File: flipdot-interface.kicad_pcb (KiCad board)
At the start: 4 copper layers, 109.2 x 88.9 mm, 100 parts, among them J1 Conn_02x30_Odd_Even, J2 Conn_02x06_Odd_Even, J3 Screw_Terminal_01x04, J4 Conn_02x06_Odd_Even, U10 74LVC1G19, U11 74HCT595, U12 ULN2803A, U13 74HCT244, U14 LM2734Y, U15 AP1117-33, U16 tle75080-esd, U17 tle75080-esd, U18 tle75080-esd, U4 74HCT595, U5 74HCT595, U6 74HCT595, U7 ULN2803A, U8 ULN2803A, U9 ULN2803A

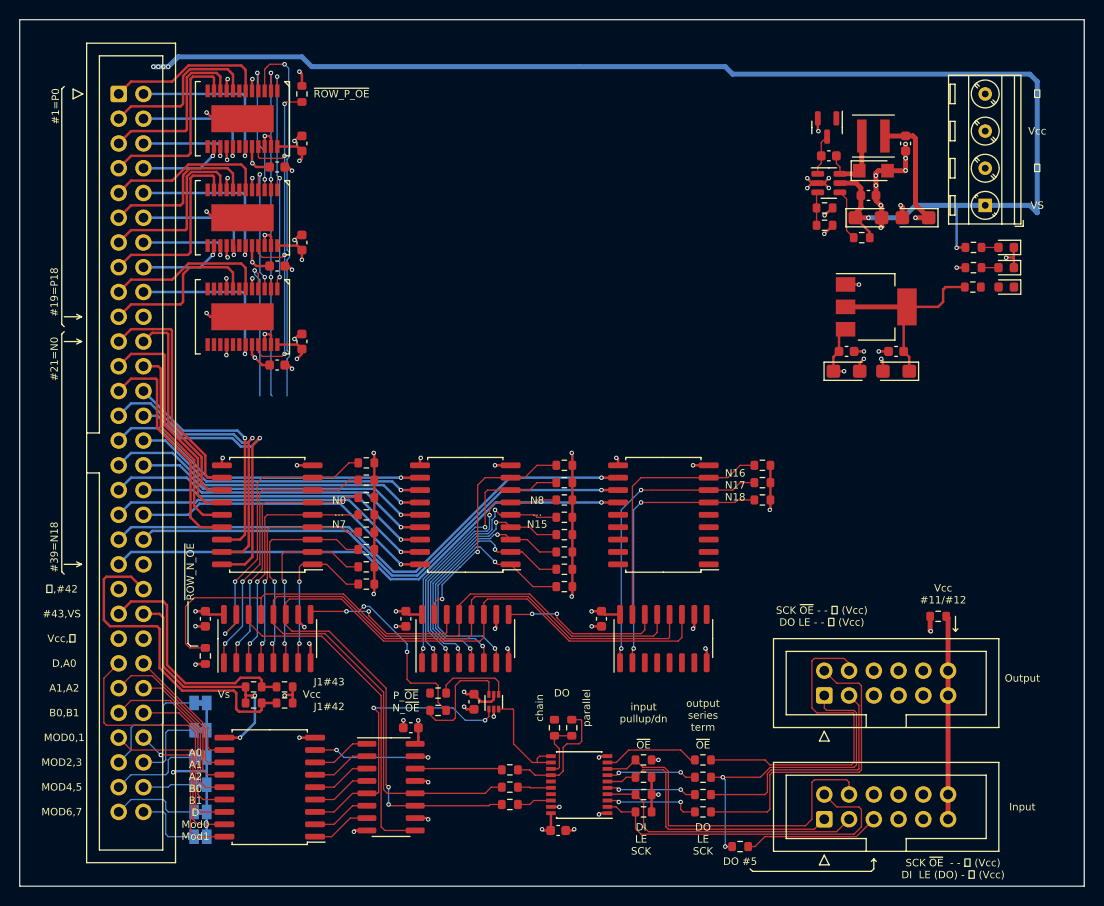
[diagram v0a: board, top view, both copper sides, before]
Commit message: Change negative drivers to a TLE75008-ESD, octal low side driver.
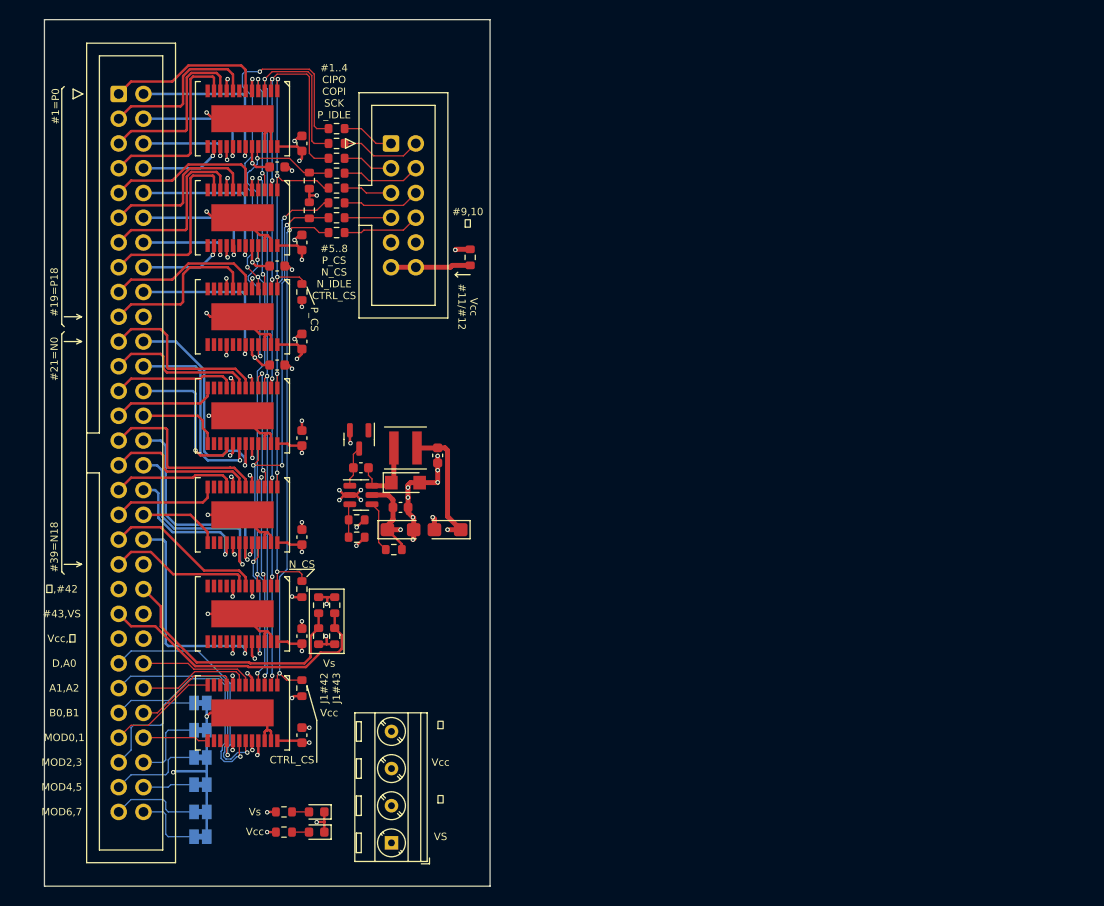
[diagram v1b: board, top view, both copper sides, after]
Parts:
- removed C10, C17, C8, C9: 100n, Capacitor_SMD:C_0603_1608Metric
- removed C16, C18: 10u, Capacitor_Tantalum_SMD:CP_EIA-3216-18_Kemet-A
- removed D24: LED, LED_SMD:LED_0603_1608Metric
- removed J2: Conn_02x06_Odd_Even, Connector_IDC:IDC-Header_2x06_P2.54mm_Vertical
- removed R100, R101, R102, R103, R104, R87, R88, R89, R90: 68R, Resistor_SMD:R_0603_1608Metric
- removed R105, R106, R108: 0R (dnp), Resistor_SMD:R_0603_1608Metric
- removed R58, R59, R60, R61, R62, R63, R64, R65, R66, R67, R68, R69, R70, R71, R72, R73, R74, R75, R76, R77, R78, R96, R97, R98, R99: 10k, Resistor_SMD:R_0603_1608Metric
- removed R79: 1k, Resistor_SMD:R_0603_1608Metric
- removed U10: 74LVC1G19, Package_TO_SOT_SMD:SOT-563
- removed U11, U5, U6: 74HCT595, Package_SO:SOIC-16_3.9x9.9mm_P1.27mm
- removed U12, U7, U8, U9: ULN2803A, Package_SO:SOIC-18W_7.5x11.6mm_P1.27mm
- removed U13: 74HCT244, Package_SO:SSOP-20_4.4x6.5mm_P0.65mm
- removed U15: AP1117-33, Package_TO_SOT_SMD:SOT-223-3_TabPin2
- added R1: 10k, Resistor_SMD:R_0603_1608Metric, F.Cu at (146.6, 59.7)
- added R10: 10k, Resistor_SMD:R_0603_1608Metric, F.Cu at (145.8, 71.1)
- added R11: 10k, Resistor_SMD:R_0603_1608Metric, F.Cu at (145.8, 101.6)
- added R12: 10k, Resistor_SMD:R_0603_1608Metric, F.Cu at (146.6, 62.7)
- added R13: 10k, Resistor_SMD:R_0603_1608Metric, F.Cu at (145.8, 111.8)
- added R2: 68R, Resistor_SMD:R_0603_1608Metric, F.Cu at (149.4, 54.4)
- added R3: 68R, Resistor_SMD:R_0603_1608Metric, F.Cu at (149.4, 58.9)
- added R4: 68R, Resistor_SMD:R_0603_1608Metric, F.Cu at (149.4, 55.9)
- added R5: 68R, Resistor_SMD:R_0603_1608Metric, F.Cu at (149.4, 57.4)
- added R6: 68R, Resistor_SMD:R_0603_1608Metric, F.Cu at (149.4, 60.5)
- added R7: 68R, Resistor_SMD:R_0603_1608Metric, F.Cu at (149.4, 62.0)
- added R8: 68R, Resistor_SMD:R_0603_1608Metric, F.Cu at (149.4, 63.5)
- added R9: 68R, Resistor_SMD:R_0603_1608Metric, F.Cu at (149.4, 65.0)
- added U1: tle75008-esd, vogelchr_package_so:Infineon-PG-TSDSO-24-51, F.Cu at (139.7, 83.8)
- added U2: tle75008-esd, vogelchr_package_so:Infineon-PG-TSDSO-24-51, F.Cu at (139.7, 94.0)
- added U3: tle75008-esd, vogelchr_package_so:Infineon-PG-TSDSO-24-51, F.Cu at (139.7, 104.1)
- U4: value 74HCT595 -> tle75008-esd; footprint Package_SO:SOIC-16_3.9x9.9mm_P1.27mm -> vogelchr_package_so:Infineon-PG-TSDSO-24-51
- moved D22 91.4 mm to (147.3, 124.5)
- moved D23 91.4 mm to (147.3, 126.5)
- moved R94 91.4 mm to (144.0, 124.5)
- moved R95 91.4 mm to (144.0, 126.5)
- moved J3 89.4 mm to (155.0, 127.6)
- moved J4 72.0 mm to (154.9, 55.9), turned to 0 degrees
- moved R107 60.5 mm to (163.1, 67.6), turned to -90 degrees
- moved C11 57.7 mm to (155.9, 93.2)
- moved C12 57.7 mm to (155.9, 95.5)
- moved C13 57.7 mm to (151.8, 89.2)
- moved C14 57.7 mm to (159.7, 87.9)
- moved C15 57.7 mm to (160.7, 95.5)
- moved D20 57.7 mm to (151.7, 86.2)
- moved D21 57.7 mm to (156.4, 90.7)
- moved L1 57.7 mm to (156.4, 87.1)
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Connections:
- net /Row Drivers Positive/~{ROW_P_CS} renamed /~{ROW_P_CS}
- net /~{ROW_P_OE} renamed /ROW_P_IDLE
- J4 pad 1: /DO -> Net-(J4-Pad1)
- J4 pad 11: Net-(J2-Pad11) -> Net-(J4-Pad11)
- J4 pad 12: Net-(J2-Pad11) -> Net-(J4-Pad11)
- J4 pad 2: /SCK_OUT -> Net-(J4-Pad2)
- J4 pad 3: /LE_OUT -> Net-(J4-Pad3)
- J4 pad 4: /~{ROW_OE}_OUT -> Net-(J4-Pad4)
- J4 pad 5: unconnected-(J4-Pad5) -> Net-(J4-Pad5)
- J4 pad 6: unconnected-(J4-Pad6) -> Net-(J4-Pad6)
- J4 pad 7: unconnected-(J4-Pad7) -> Net-(J4-Pad7)
- J4 pad 8: unconnected-(J4-Pad8) -> Net-(J4-Pad8)
- R107 pad 1: Net-(J2-Pad11) -> VCC
- R107 pad 2: VCC -> Net-(J4-Pad11)
- U16 pad 3: /ROW_DI -> /COPI
- U18 pad 4: /DO_P -> /CIPO
- U4 pad 1: /Row Drivers Negative/ROW_N_G1 -> /CTRL_CS
- U4 pad 10: VCC -> unconnected-(U4-Pad10)
- U4 pad 11: /SCK -> unconnected-(U4-Pad11)
- U4 pad 12: /LE -> /MODULE_A0
- U4 pad 13: /~{ROW_N_OE} -> /MODULE_A1
- U4 pad 14: /ROW_DI -> unconnected-(U4-Pad14)
- U4 pad 15: /Row Drivers Negative/ROW_N_G0 -> unconnected-(U4-Pad15)
- U4 pad 16: VCC -> /COL_D
- U4 pad 2: /Row Drivers Negative/ROW_N_G2 -> /SCK
- U4 pad 3: /Row Drivers Negative/ROW_N_G3 -> /COPI
- U4 pad 4: /Row Drivers Negative/ROW_N_G4 -> /CIPO
- U4 pad 5: /Row Drivers Negative/ROW_N_G5 -> GND
- U4 pad 6: /Row Drivers Negative/ROW_N_G6 -> /COL_A0
- U4 pad 7: /Row Drivers Negative/ROW_N_G7 -> /COL_A2
- U4 pad 9: Net-(U4-Pad9) -> /COL_B1
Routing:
- net VS: track 185.1 -> 94.1 mm, vias 20 -> 16
- net /LE: track 89.8 -> 0.00 mm
- net /CIPO: track 0.00 -> 82.7 mm, vias 0 -> 5
- net /~{ROW_N_OE}: track 82.4 -> 0.00 mm, vias 2 -> 0
- net /COPI: track 0.00 -> 78.7 mm, vias 0 -> 3
- net /ROW_DI: track 73.0 -> 0.00 mm, vias 1 -> 0
- net /ROW_N_IDLE: track 0.00 -> 58.0 mm, vias 0 -> 5
- net /CTRL_CS: track 0.00 -> 54.1 mm, vias 0 -> 2
- net /~{ROW_N_CS}: track 0.00 -> 49.5 mm, vias 0 -> 4
- net /SCK: track 127.1 -> 82.5 mm, vias 5 -> 7
- net /Row Drivers Negative/ROW_N18: track 56.2 -> 14.9 mm, vias 1 -> 0
- net /Row Drivers Negative/ROW_N16: track 57.6 -> 16.6 mm, vias 1 -> 0
- net /~{ROW_OE}_LV: track 36.8 -> 0.00 mm
- net /SCK_LV: track 34.8 -> 0.00 mm
- net /DO: track 33.5 -> 0.00 mm, vias 2 -> 0
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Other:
- board size 109.2 x 88.9 mm -> 45.7 x 88.9 mm
- board text added: "#1..4 CIPO COPI SCK P_IDLE"
- board text added: "#5..8 P_CS N_CS N_IDLE CTRL_CS"
- board text added: "#9,10 ⏚"
- board text added: "CTRL_CS"
- board text added: "N_CS"
- board text added: "P_CS"
- board text removed: "A0 A1 A2 B0 B1 D Mod0 Mod1"
- board text removed: "DI LE SCK"
- board text removed: "DO"
- board text removed: "DO #5"
- board text removed: "DO LE SCK"
- board text removed: "Input"
- board text removed: "N0 ... N7"
- board text removed: "N16 N17 N18"
- board text removed: "N8 ... N15"
- board text removed: "N_~{OE}"
- board text removed: "Output"
- board text removed: "P_~{OE}"
- board text removed: "SCK ~{OE} - - ⏚ (Vcc) DI LE (DO) - ⏚ (Vcc)"
- board text removed: "SCK ~{OE} - - ⏚ (Vcc) DO LE - - ⏚ (Vcc)"
- board text removed: "chain"
- board text removed: "input pullup/dn"
- board text removed: "output series term"
- board text removed: "parallel"
- board text removed: "~{OE}"
- board text removed: "~{ROW_N_OE}"
- board text removed: "~{ROW_P_OE}"
